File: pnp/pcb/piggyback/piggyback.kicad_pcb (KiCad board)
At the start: 2 copper layers, 124.5 x 86.4 mm, 94 parts, among them J1 STEPPER_1, J10 F06, J11 F07, J12 F08, J13 F09, J14 F10, J15 F11, J16 F12, J17 F13, J18 F14, J19 F15, J2 STEPPER_2, J20 F16, J21 F17, J22 F18, J23 F19, J24 F20, J25 F25, J26 F26, J27 F27, J28 F28, J29 F21, J3 STEPPER_3, J30 F22, J31 F23, J32 F24, J33 F29, J34 F30, J35 F31, J36 F32, J37 Screw_Terminal_01x03, J38 AVR-ISP-6, J39 SERIAL_INTERFACE, J4 USB_B_Micro, J5 F01, J6 F02, J7 F03, J8 F04, J9 F05, U1 MCP23017_SO_2, U2 ATmega32U4-AU, U3 MCP23017_SO_3, U4 MCP23017_SO_1, U5 MCP23017_SO_4, Y1 16MHz

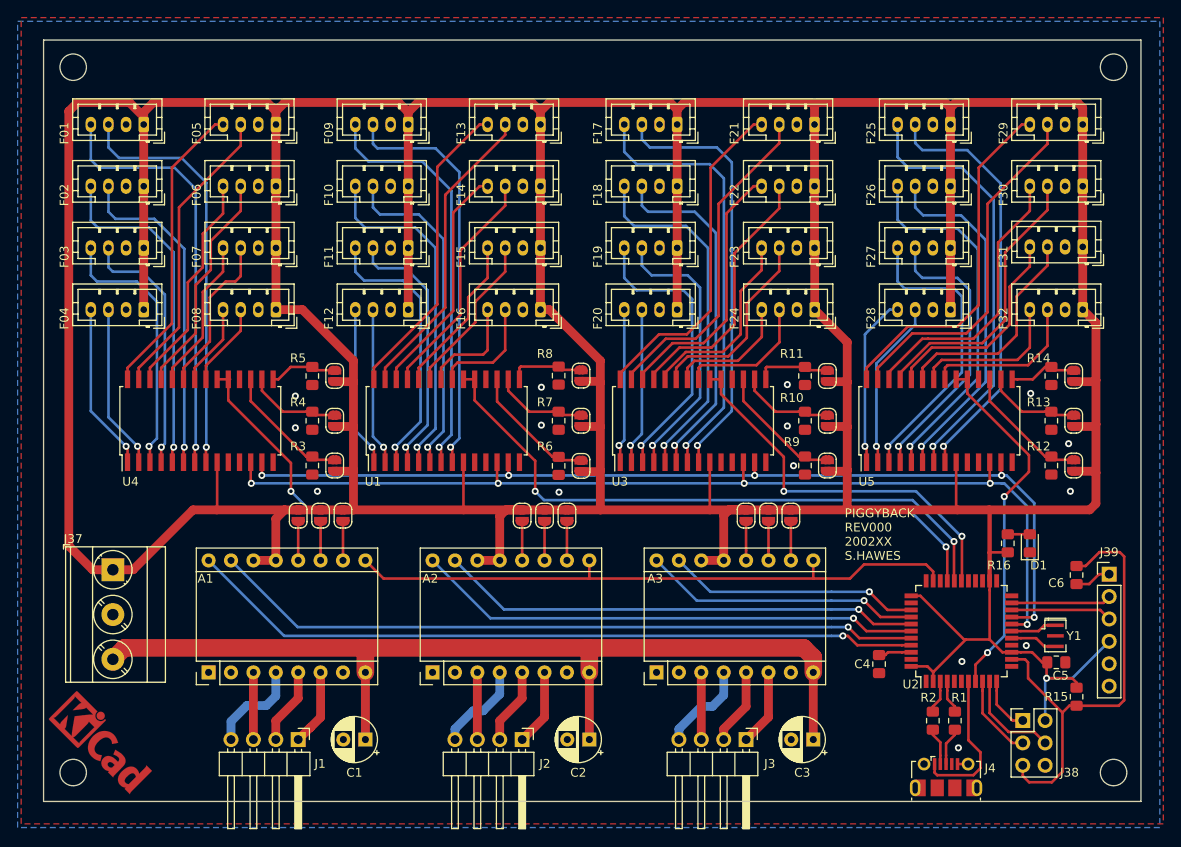
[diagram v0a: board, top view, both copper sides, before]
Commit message: Adding feeder and pnp CAD, updating Piggyback to fix USB, MCP23017 Reset pullup, and add uC reset button.
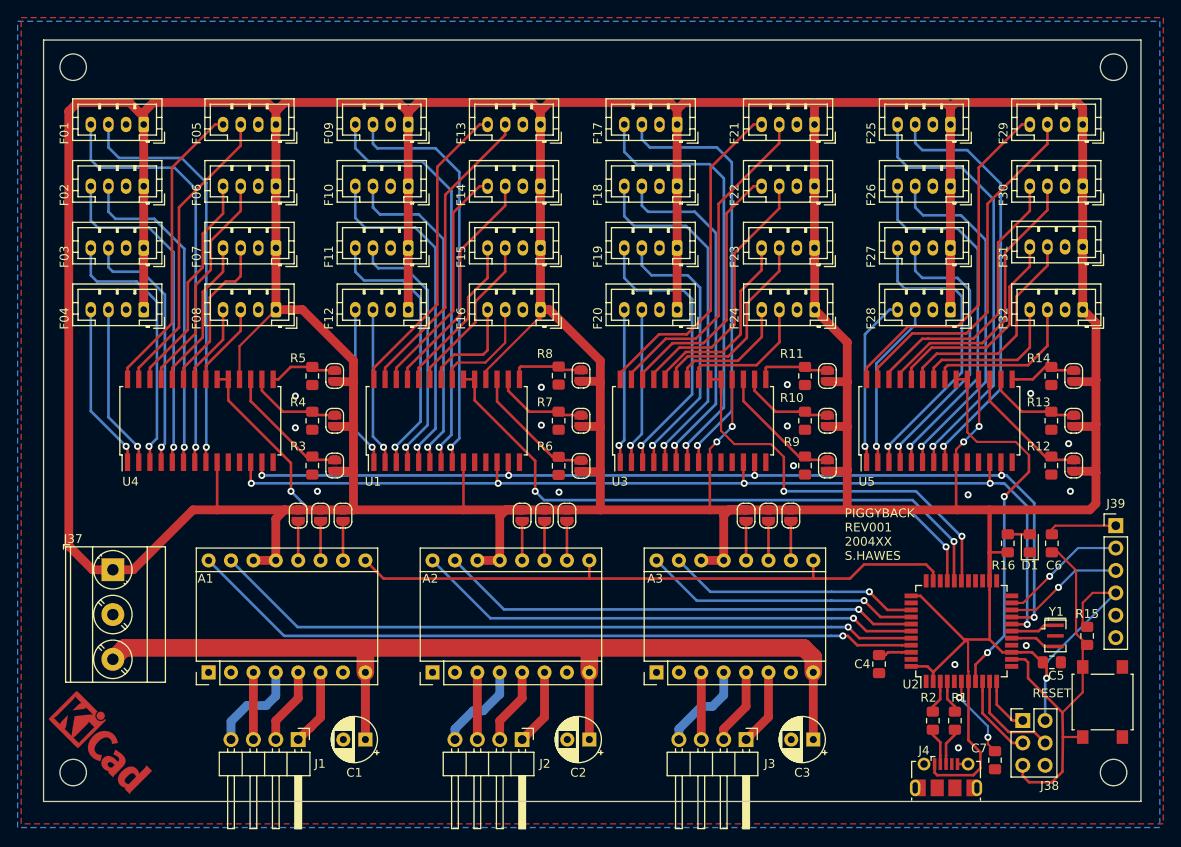
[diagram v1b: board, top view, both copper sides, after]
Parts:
- added C7: 1uF, Capacitor_SMD:C_0805_2012Metric_Pad1.15x1.40mm_HandSolder, F.Cu at (148.6, 140.1)
- added SW1: SW_Push_Dual, Button_Switch_SMD:SW_SPST_B3S-1000, F.Cu at (160.8, 133.5)
- moved R15 7.00 mm to (159.0, 126.0)
- moved J39 5.55 mm to (162.2, 113.5)
- moved C6 4.56 mm to (155.0, 115.5), turned to 90 degrees
- moved C5 0.50 mm to (155.0, 129.0)
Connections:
- J4 pad 1: Net-(J4-Pad1) -> +5V
- U1 pad 18: Net-(U1-Pad18) -> +5V
- U2 pad 7: Net-(J4-Pad1) -> +5V
- U3 pad 18: Net-(U3-Pad18) -> +5V
- U4 pad 18: Net-(U4-Pad18) -> +5V
- U5 pad 18: Net-(U5-Pad18) -> +5V
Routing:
- net +5V: track 717.5 -> 787.3 mm, vias 1 -> 5
- net Net-(J4-Pad1): track 17.0 -> 0.00 mm
- net Net-(C7-Pad2): track 0.00 -> 9.69 mm, vias 0 -> 2
- net RESET: track 52.7 -> 46.2 mm
- net DTR: track 4.17 -> 7.99 mm
- net TX: track 11.4 -> 14.4 mm, vias 0 -> 1
- net 4_INT: track 40.9 -> 43.5 mm
- net 3_INT: track 44.3 -> 46.7 mm
- net RX: track 11.5 -> 13.7 mm, vias 0 -> 1
- net GND: vias 15 -> 16
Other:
- board text added: "PIGGYBACK REV001 2004XX S.HAWES"
- board text added: "RESET"
- board text removed: "PIGGYBACK REV000 2002XX S.HAWES"
